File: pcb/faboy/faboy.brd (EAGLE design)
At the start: 85.1 x 54 mm, 57 parts, among them U1 MAX1595UMAX, U2 MCP73831, Y1 16MHZ

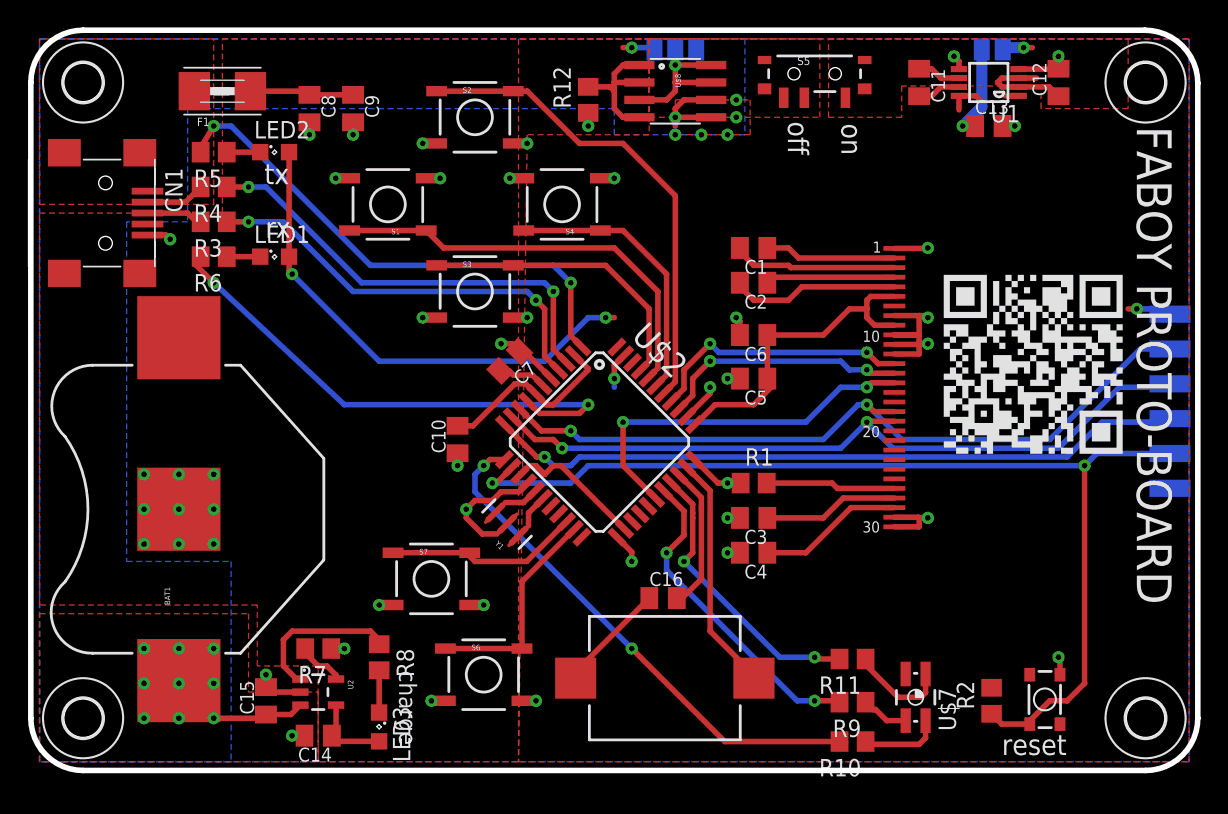
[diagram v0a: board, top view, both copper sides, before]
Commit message: change the usb connector to micro B
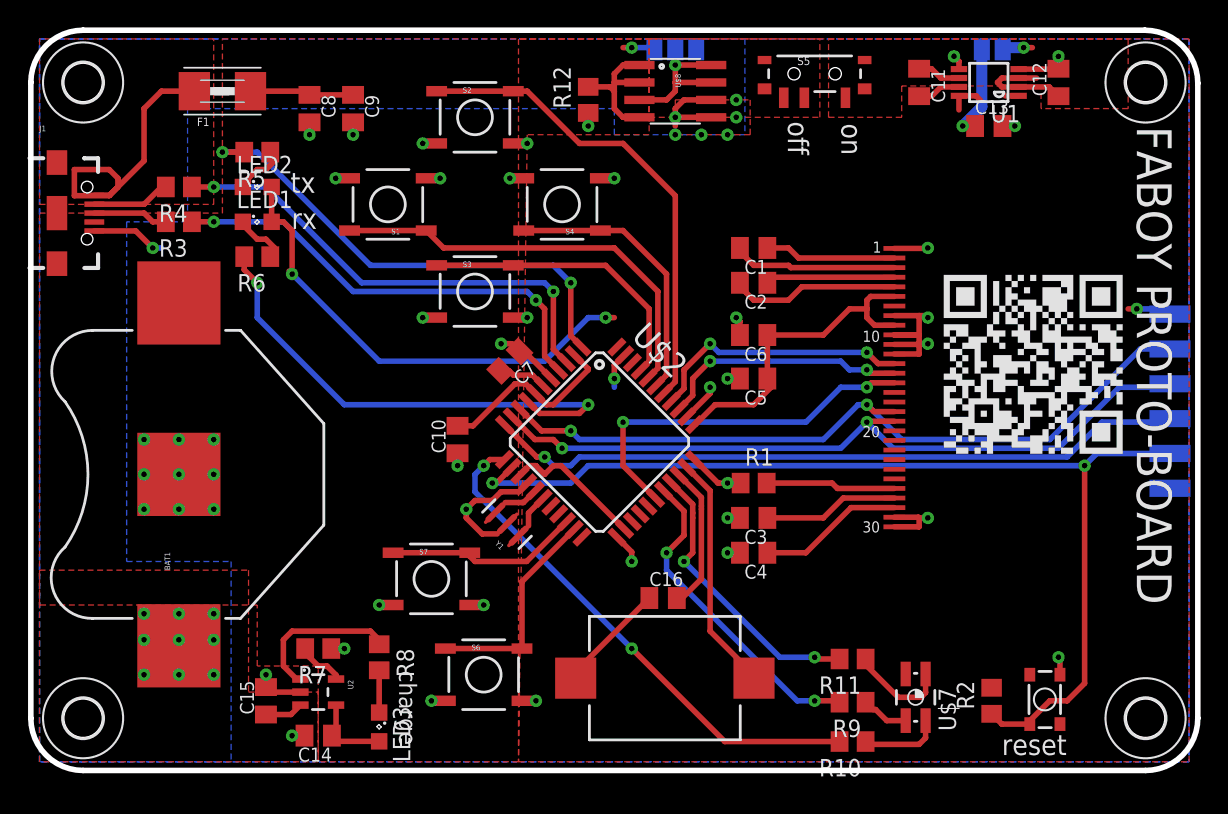
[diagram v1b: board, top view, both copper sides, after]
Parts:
- removed CN1: (no value), adafruit:USB-MINIB
- added J1: USB-MICROBREDUCED_PASTE, SparkFun-Connectors:USB-B-MICRO-SMD_V03_RED_PASTE
- moved R5 3.18 mm to (16.5, 45.1)
- moved R6 3.18 mm to (16.5, 37.5)
- moved LED1 2.84 mm to (16.5, 40.0)
- moved LED2 2.84 mm to (16.5, 42.5)
- moved R3 2.54 mm to (10.8, 40.0)
- moved R4 2.54 mm to (10.8, 42.5)
- moved BAT1 2.54 mm to (10.8, 21.6)
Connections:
- net GND: now also J1.GND; no longer CN1.GND
- net N$12: now also J1.D+; no longer CN1.D+
- net N$13: now also J1.D-; no longer CN1.D-
- net VBUS: now also J1.VBUS; no longer CN1.VBUS
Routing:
- net VBUS: track 0.00 -> 22.1 mm
- net VBAT: track 17.3 -> 10.4 mm
- net GND: track 80.8 -> 84.4 mm
- net D+: track 30.7 -> 33.3 mm
- net D-: track 32.6 -> 35.1 mm
- net LED_RX: track 38.4 -> 36.6 mm
- net LED_TX: track 38.0 -> 36.3 mm
- net N$25: track 2.45 -> 4.01 mm
- net N$23: track 2.45 -> 4.01 mm
- net N$13: track 4.33 -> 5.73 mm
- net VCC: track 85.9 -> 84.7 mm
